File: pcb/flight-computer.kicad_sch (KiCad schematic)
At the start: 0 parts

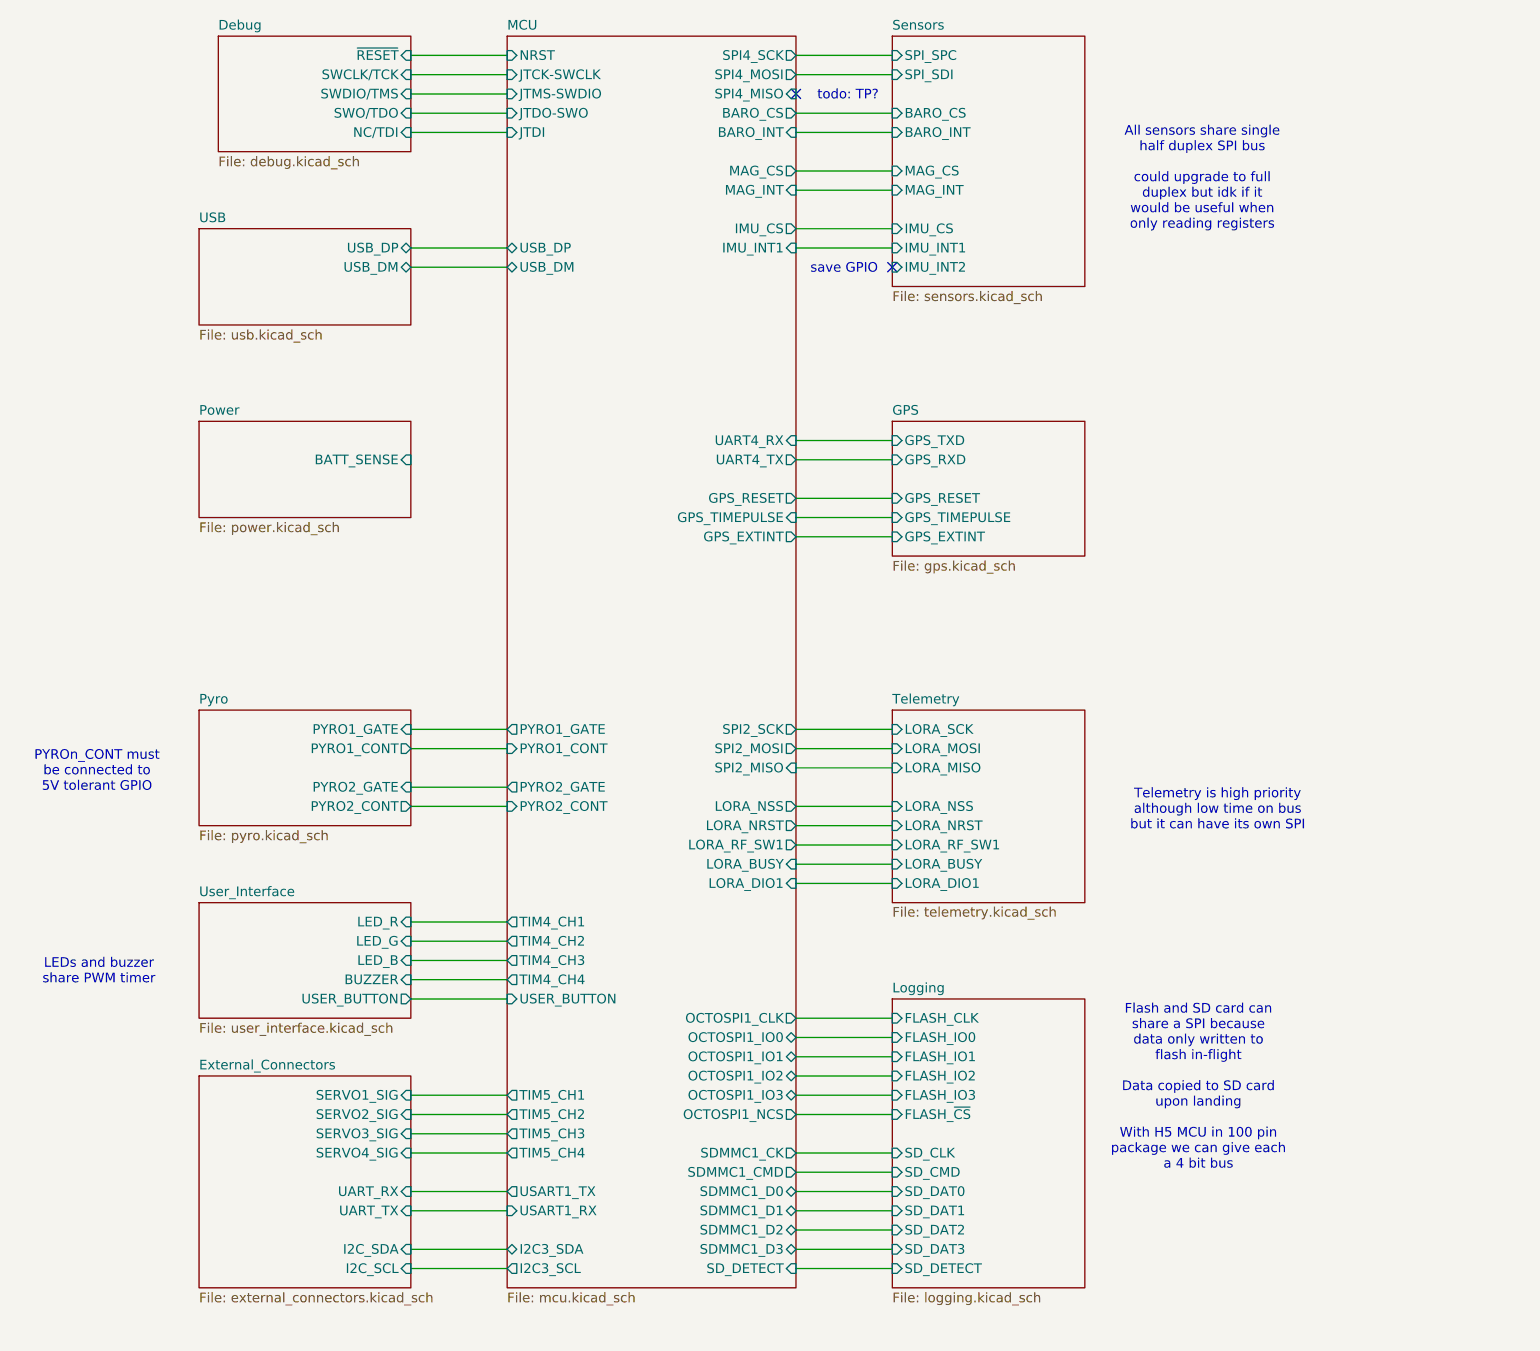
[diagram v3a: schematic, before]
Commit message: Fix pin directionality
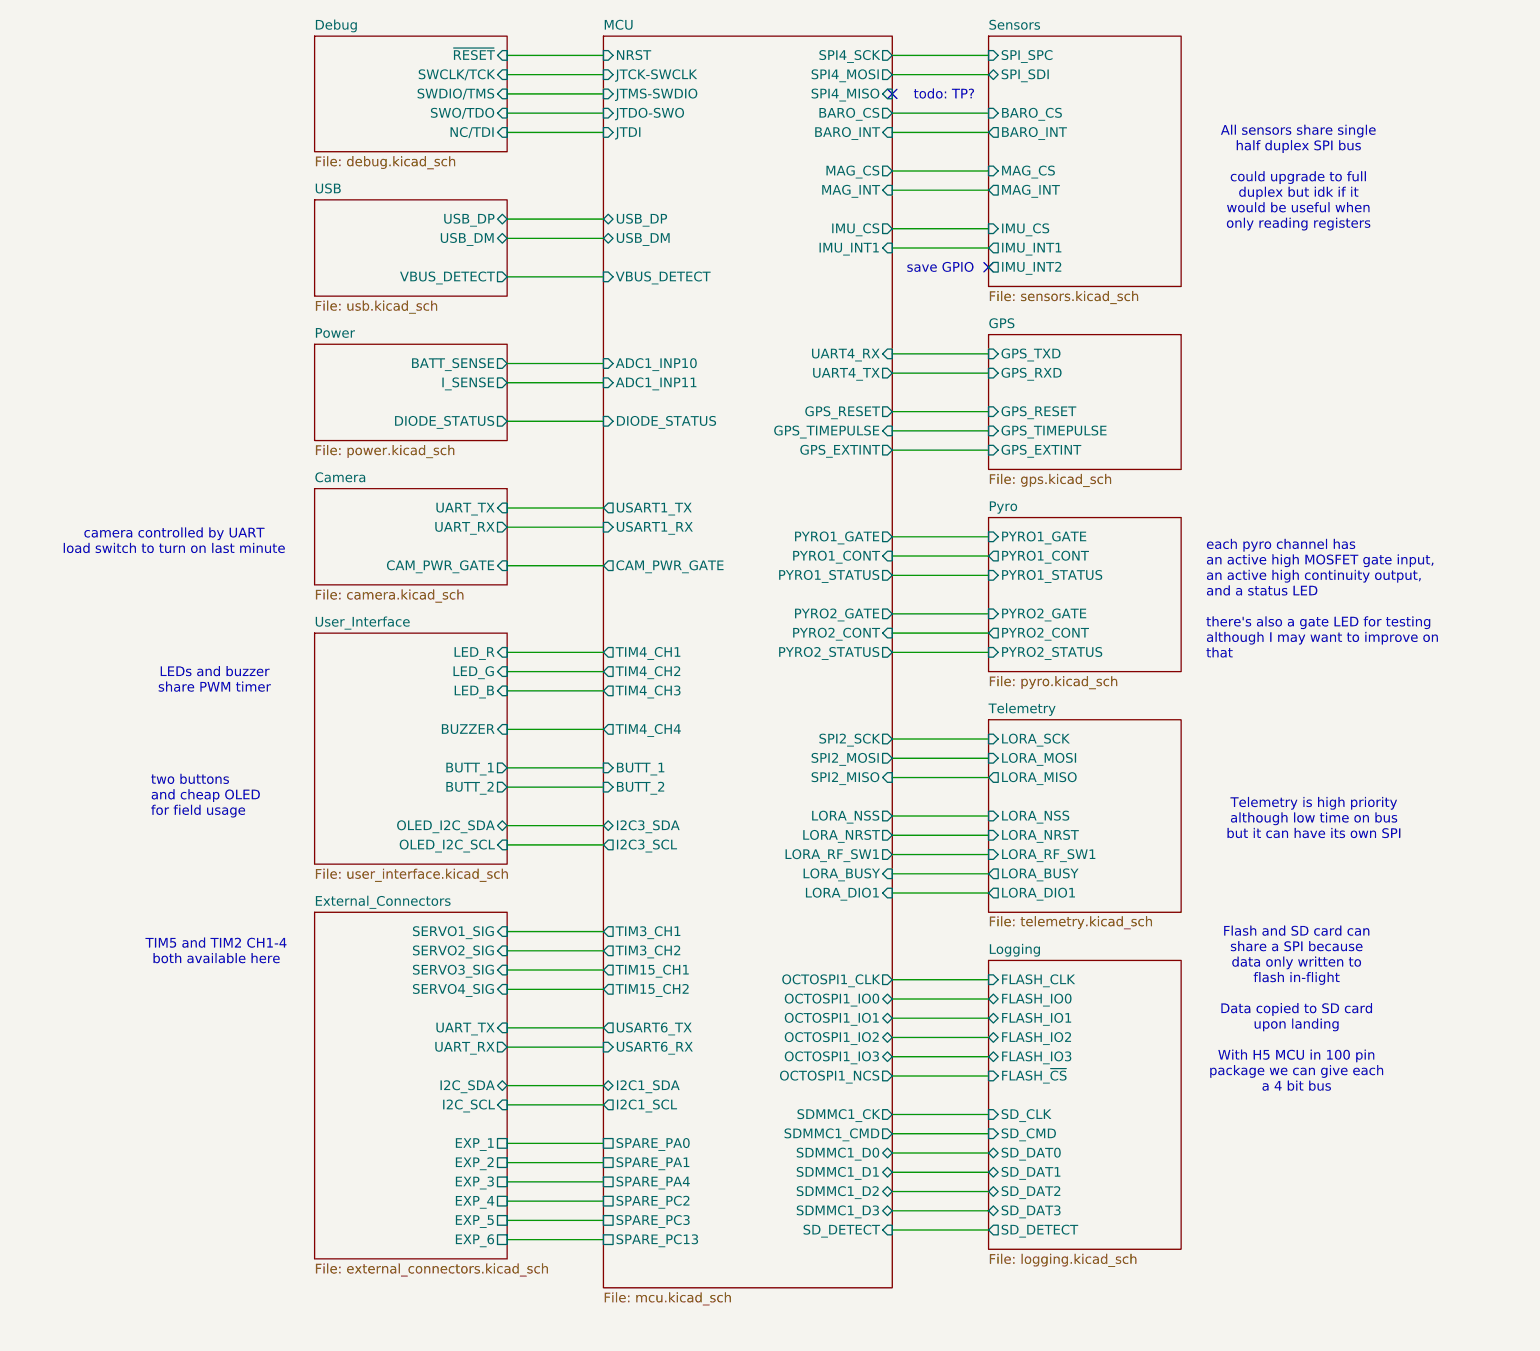
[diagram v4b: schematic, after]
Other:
- added sheet Camera (camera.kicad_sch)
- sheet External_Connectors ports: added EXP_1, EXP_2, EXP_3, EXP_4, EXP_5, EXP_6; removed none
- sheet MCU ports: added ADC1_INP10, ADC1_INP11, BUTT_1, BUTT_2, CAM_PWR_GATE, DIODE_STATUS, I2C1_SCL, I2C1_SDA, PYRO1_STATUS, PYRO2_STATUS, SPARE_PA0, SPARE_PA1, SPARE_PA4, SPARE_PC13, SPARE_PC2, SPARE_PC3, TIM15_CH1, TIM15_CH2, TIM3_CH1, TIM3_CH2, USART6_RX, USART6_TX, VBUS_DETECT; removed TIM5_CH1, TIM5_CH2, TIM5_CH3, TIM5_CH4, USER_BUTTON
- sheet Power ports: added DIODE_STATUS, I_SENSE; removed none
- sheet Pyro ports: added PYRO1_STATUS, PYRO2_STATUS; removed none
- sheet USB ports: added VBUS_DETECT; removed none
- sheet User_Interface ports: added BUTT_1, BUTT_2, OLED_I2C_SCL, OLED_I2C_SDA; removed USER_BUTTON
- note added: "TIM5 and TIM2 CH1-4 both available here"
- note added: "camera controlled by UART load switch to turn on last minute"
- note added: "each pyro channel has an active high MOSFET gate input, an active high continuity output, and a status LED there's also a gate LED for testing although I may want to improve on that"
- note added: "two buttons and cheap OLED for field usage"
- note removed: "PYROn_CONT must be connected to 5V tolerant GPIO"
